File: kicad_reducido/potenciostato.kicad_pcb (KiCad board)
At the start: 2 copper layers, 150 x 100 mm, 35 parts, among them J1 Conn_01x03_Female, J2 USB_B_Micro, J3 Conn_01x03_Male, U1 OP77, U2 TL082, U3 OP77, U4 OP77, U7 TL064

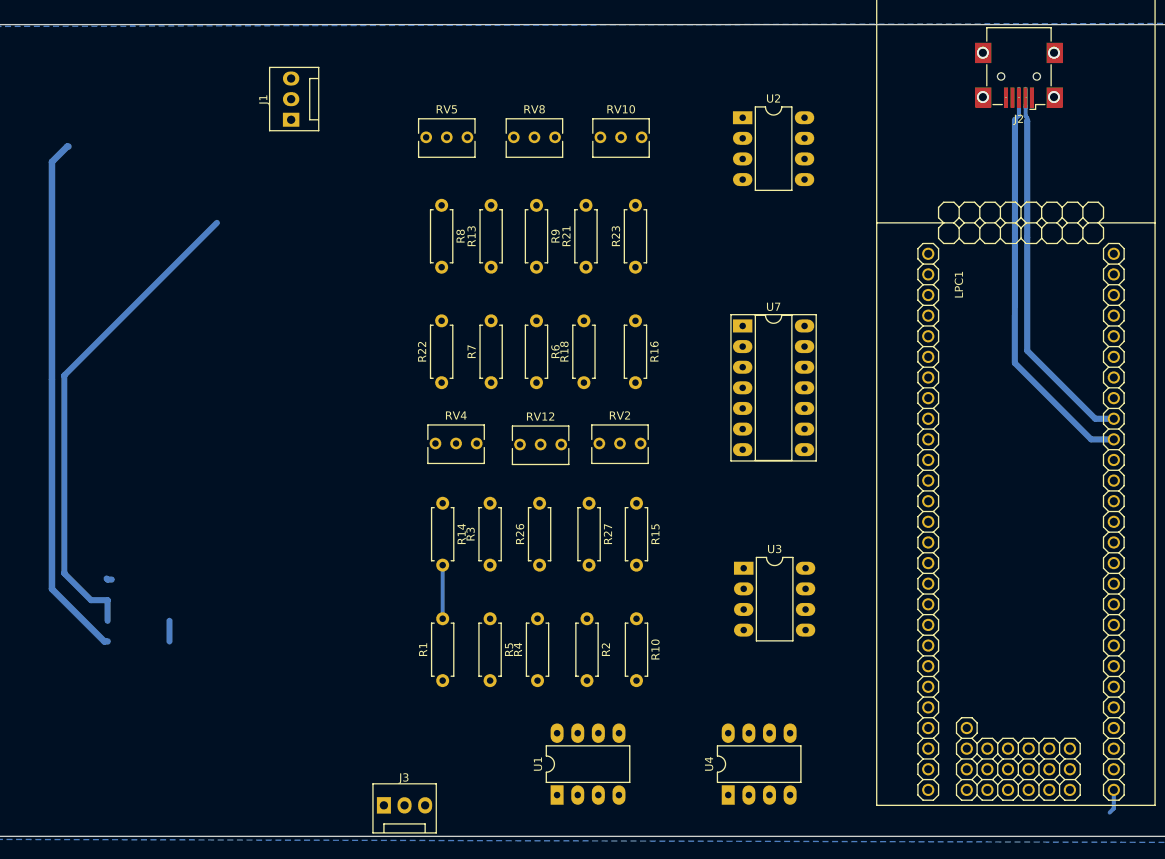
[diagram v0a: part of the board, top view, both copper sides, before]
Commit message: ruteado kicad reducido parcialmente completo
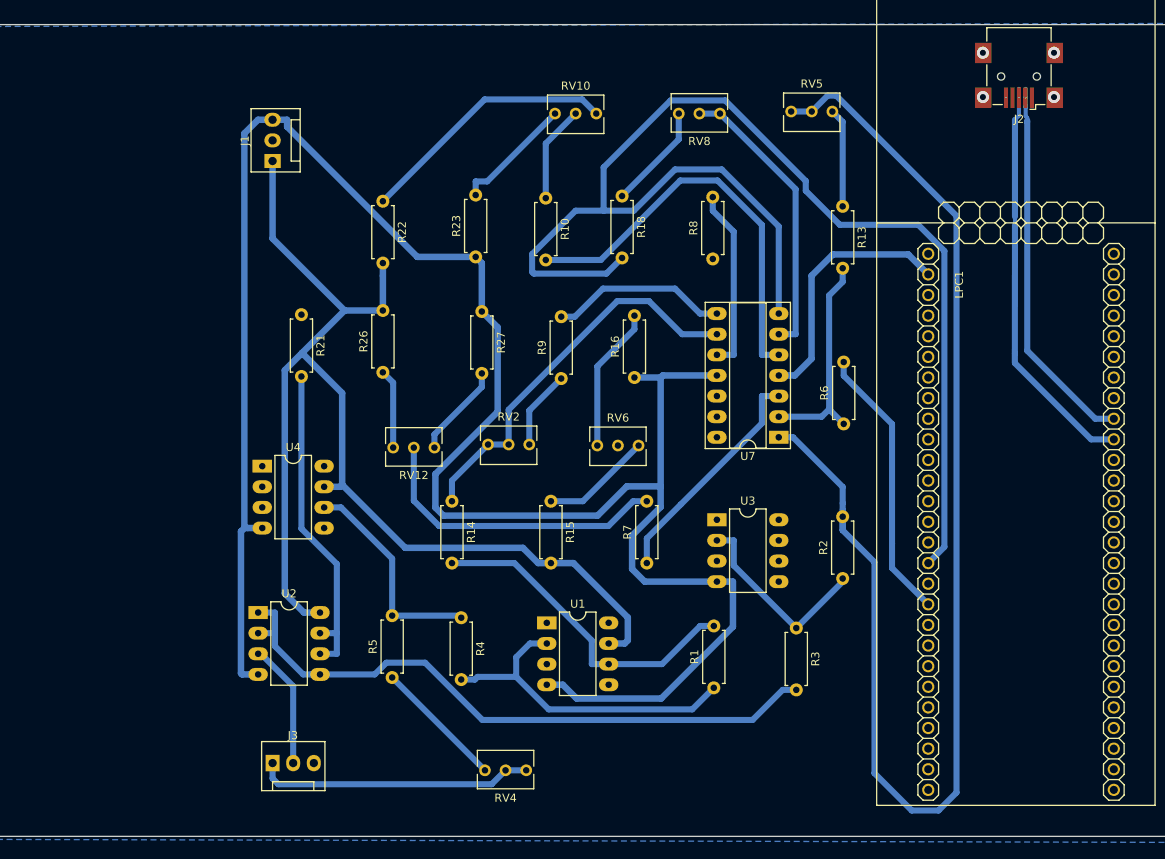
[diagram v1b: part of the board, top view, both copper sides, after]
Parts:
- added RV6: 1K, Potentiometer_THT:Potentiometer_Bourns_3266Y_Vertical, F.Cu at (730.9, 54.4)
- moved U2 85.3 mm to (684.0, 74.9)
- moved U4 70.3 mm to (684.5, 56.9), turned to 0 degrees
- moved R10 53.0 mm to (719.5, 23.9)
- moved RV5 45.1 mm to (754.8, 13.2)
- moved R13 44.0 mm to (756.0, 24.9), turned to 270 degrees
- moved RV4 40.3 mm to (712.0, 94.4), turned to 180 degrees
- moved R6 39.9 mm to (756.2, 51.7), turned to 90 degrees
- moved R3 38.5 mm to (750.3, 76.8), turned to 270 degrees
- moved R21 35.5 mm to (689.4, 38.2), turned to 270 degrees
- moved R8 34.0 mm to (740.0, 31.4), turned to 90 degrees
- moved R1 33.4 mm to (740.2, 84.2)
- moved R2 31.9 mm to (756.0, 70.7), turned to 90 degrees
- moved R26 30.6 mm to (699.4, 45.3)
- moved R7 29.4 mm to (731.9, 68.8)
- moved R27 27.1 mm to (711.6, 37.8)
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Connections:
- LPC1 pad 1: GND -> (no net)
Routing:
- net -5V: track 0.00 -> 253.8 mm
- net /LPC/ADC1: track 0.00 -> 160.9 mm
- net /salida_dac/VIN: track 0.00 -> 160.3 mm
- net +5V: track 65.0 -> 175.4 mm
- net Net-(R3-Pad2): track 3.23 -> 79.0 mm
- net Net-(R10-Pad2): track 0.00 -> 51.0 mm
- net Net-(R14-Pad1): track 0.00 -> 48.5 mm
- net Net-(R10-Pad1): track 60.2 -> 11.9 mm
- net Net-(R1-Pad1): track 0.00 -> 40.9 mm
- net /salida_dac/V_IN: track 0.00 -> 40.1 mm
- net Net-(R7-Pad2): track 0.00 -> 37.8 mm
- net Net-(R21-Pad1): track 0.00 -> 35.7 mm
- net /salida_dac/I_IN: track 6.60 -> 41.1 mm
- net /LPC/DAC: track 0.00 -> 34.2 mm
- net Net-(J3-Pad1): track 0.00 -> 34.1 mm
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
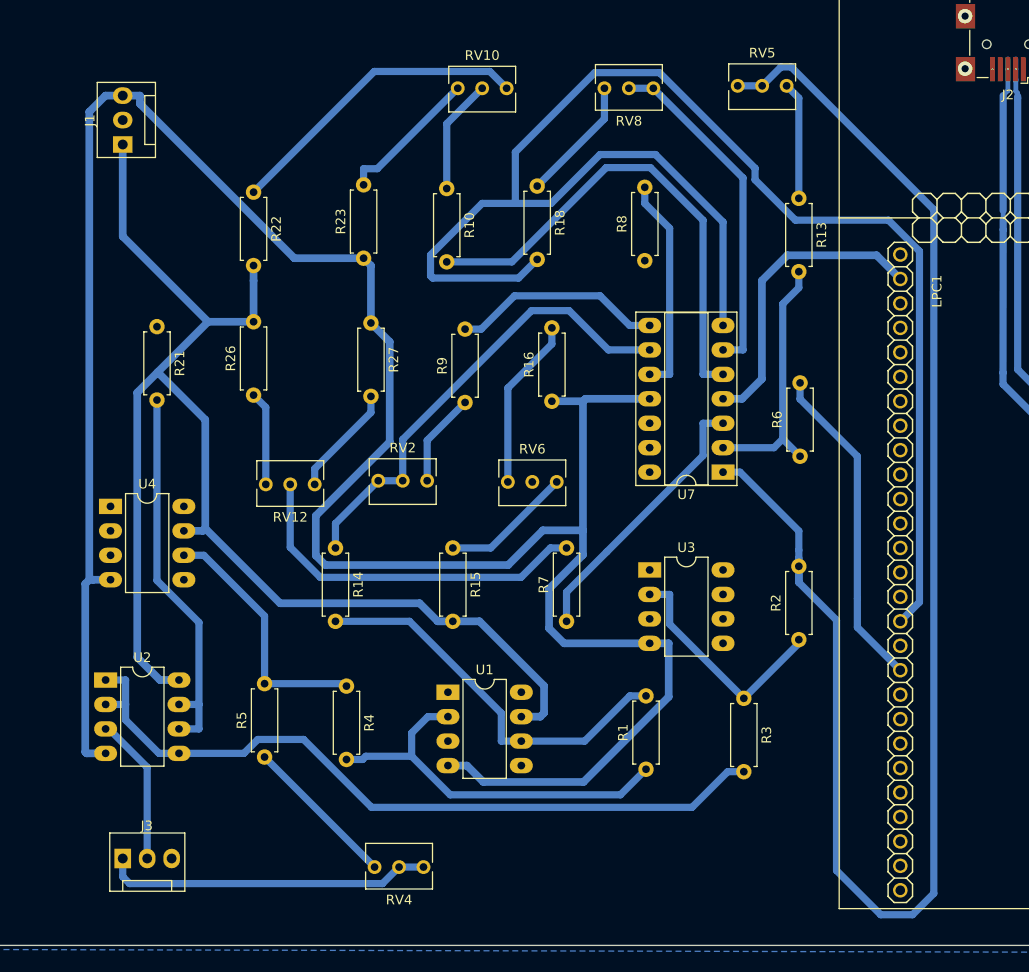
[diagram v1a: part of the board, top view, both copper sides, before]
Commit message: ruteando kicad reducido parte 2
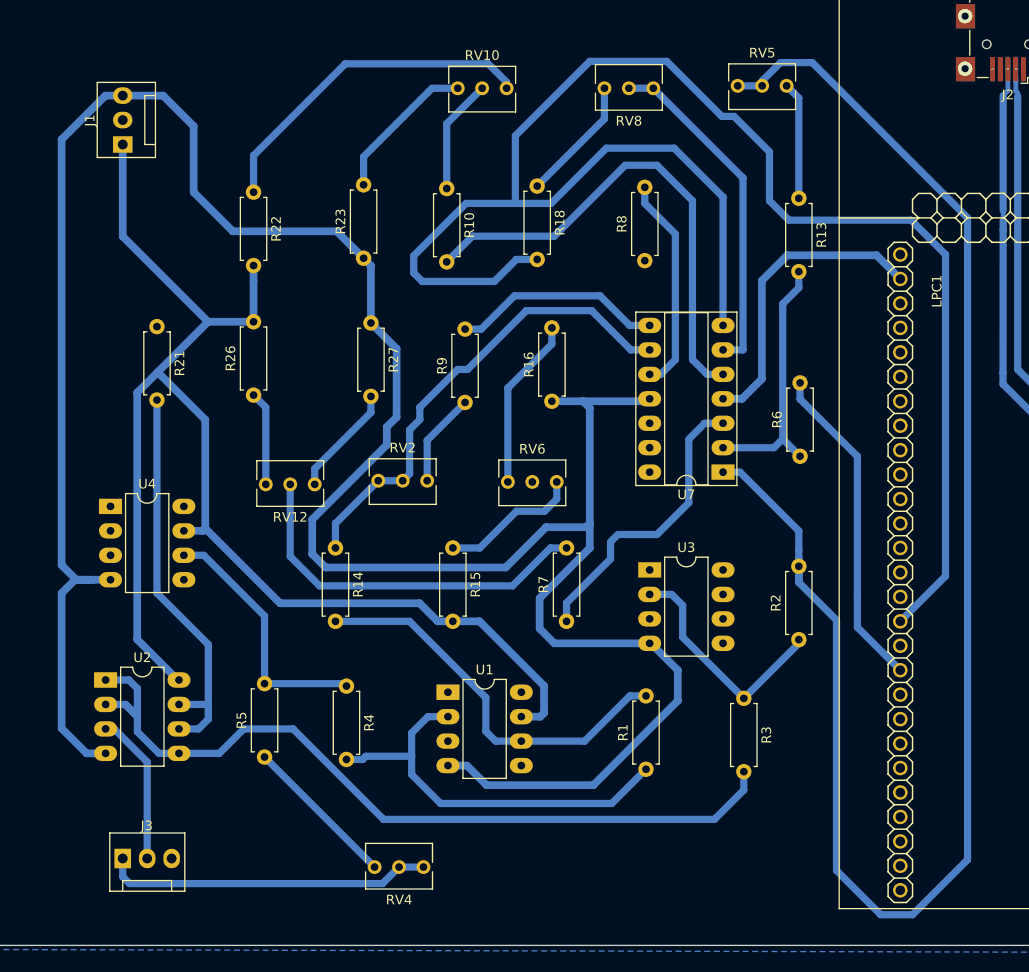
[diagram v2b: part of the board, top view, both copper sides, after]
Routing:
- net -5V: track 253.8 -> 268.3 mm
- net /LPC/ADC1: track 160.9 -> 174.4 mm
- net Net-(R3-Pad2): track 79.0 -> 85.8 mm
- net /salida_dac/VIN: track 160.3 -> 165.4 mm
- net Net-(R22-Pad1): track 32.2 -> 35.5 mm
- net Net-(R7-Pad1): track 28.5 -> 30.6 mm
- net Net-(R1-Pad1): track 40.9 -> 42.8 mm
- net /salida_dac/V_IN: track 40.1 -> 41.8 mm
- net Net-(R7-Pad2): track 37.8 -> 39.1 mm
- net +5V: track 175.4 -> 174.3 mm
- net Net-(R15-Pad1): track 13.6 -> 14.7 mm
- net Net-(R14-Pad1): track 48.5 -> 49.5 mm
- net Net-(R23-Pad2): track 14.9 -> 15.6 mm

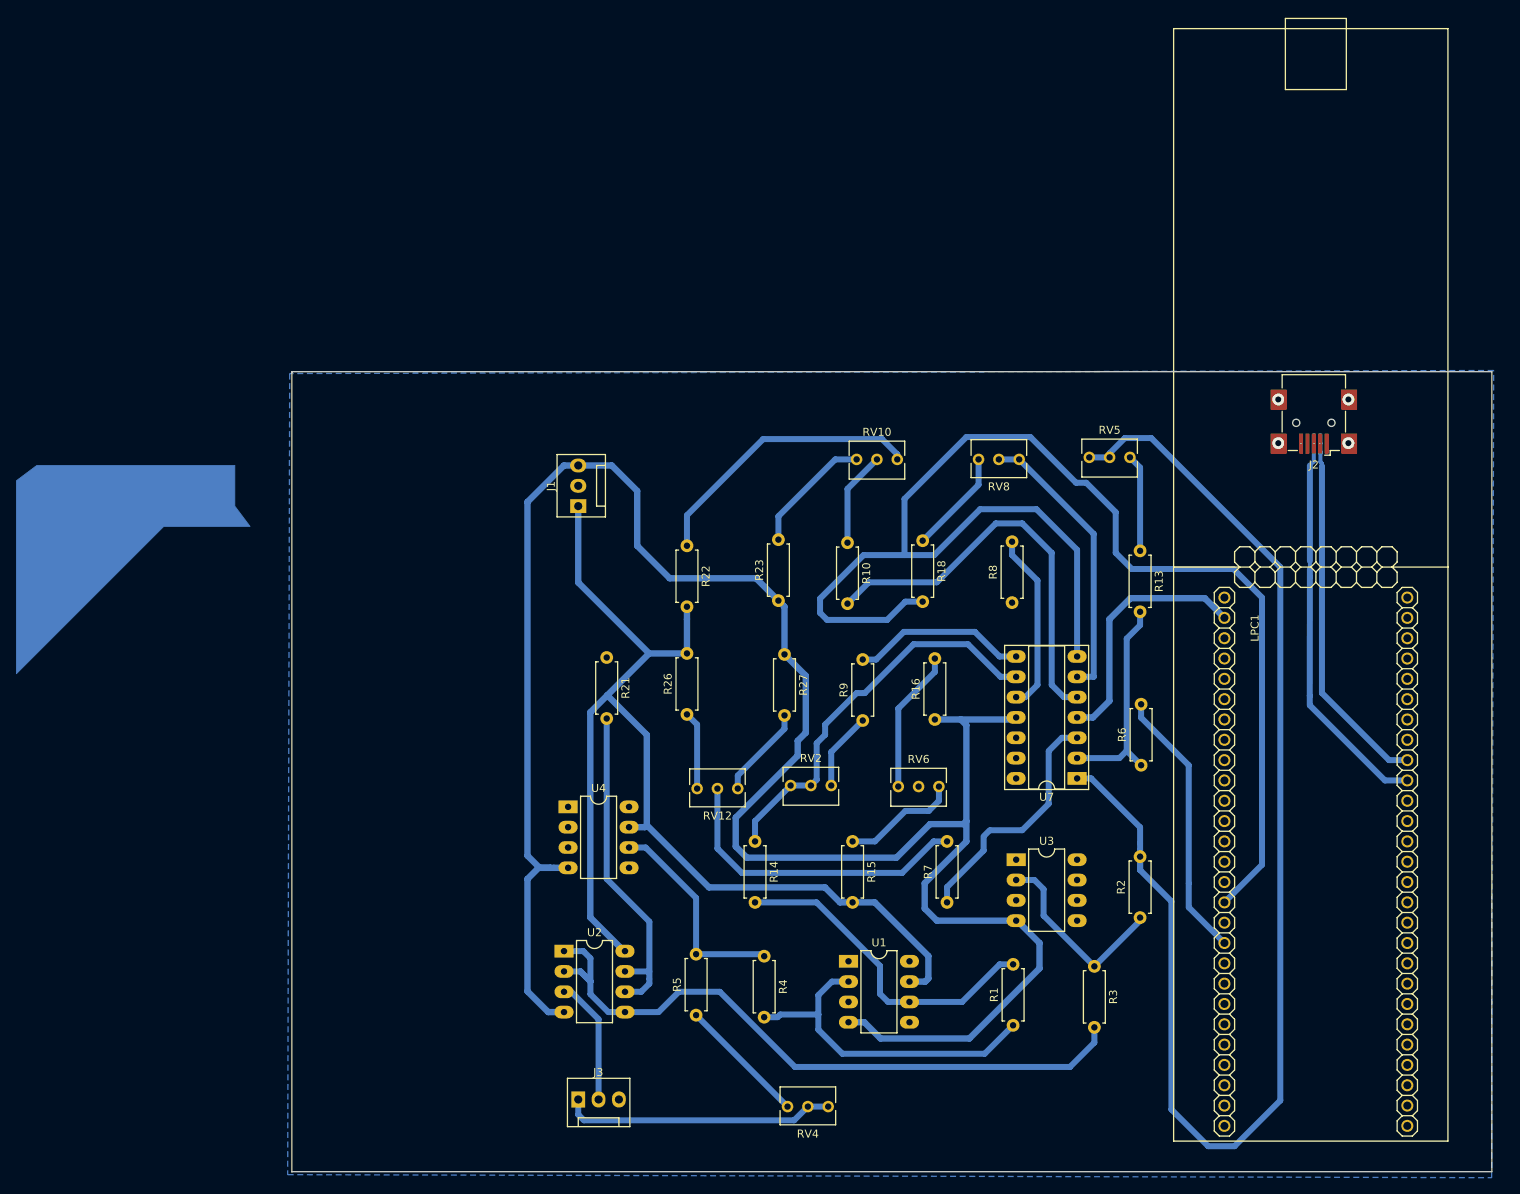
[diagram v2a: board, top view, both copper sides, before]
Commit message: pcb reducido en 10x10
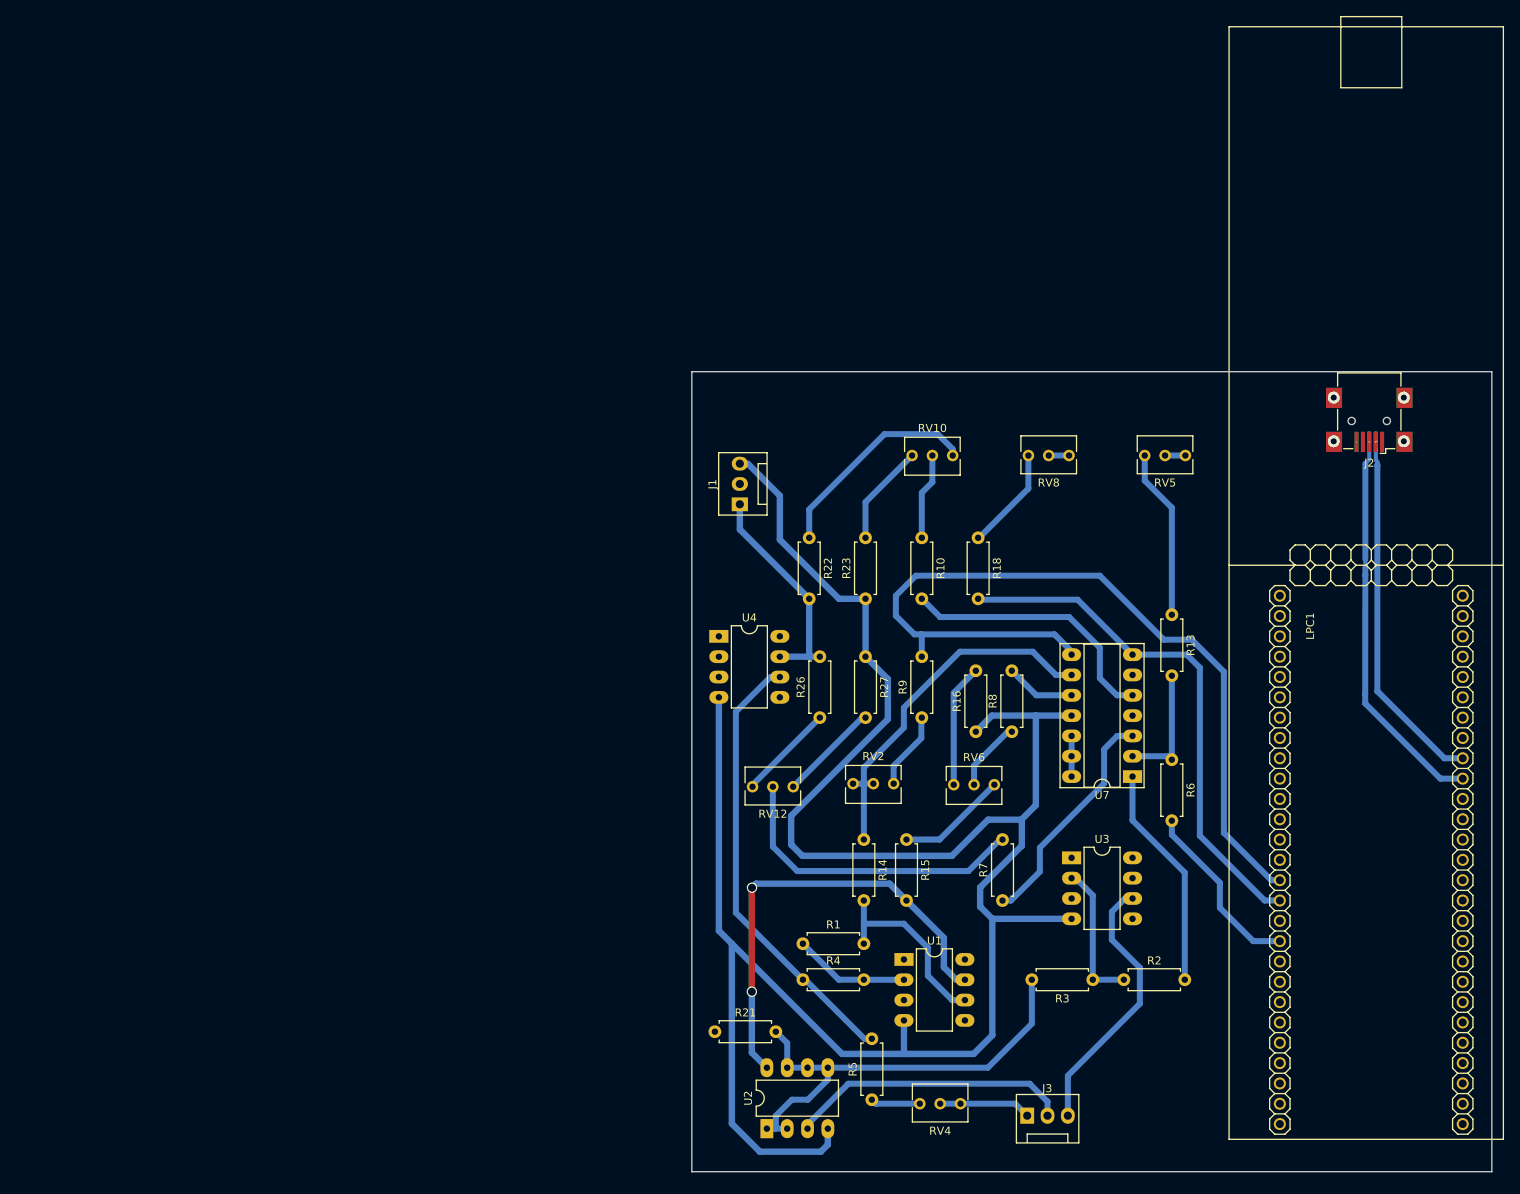
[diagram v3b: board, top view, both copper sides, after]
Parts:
- moved J3 56.2 mm to (741.9, 95.5)
- moved R21 48.7 mm to (702.9, 85.0), turned to 0 degrees
- moved U2 33.7 mm to (709.4, 97.1), turned to 90 degrees
- moved U4 28.5 mm to (703.4, 35.6)
- moved R1 28.2 mm to (713.9, 74.0), turned to 0 degrees
- moved R5 24.4 mm to (722.5, 93.5)
- moved J1 20.2 mm to (706.0, 19.1)
- moved R26 16.6 mm to (716.0, 45.7)
- moved RV4 16.5 mm to (728.5, 94.0)
- moved R8 16.1 mm to (740.0, 47.5)
- moved R22 15.3 mm to (714.7, 23.3)
- moved R14 13.6 mm to (721.5, 61.0)
- moved R23 10.9 mm to (721.7, 30.9)
- moved R27 10.1 mm to (721.7, 38.1)
- moved R10 9.31 mm to (728.7, 23.3)
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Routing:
- net /salida_dac/VIN: track 165.4 -> 30.6 mm
- net /LPC/ADC1: track 174.4 -> 65.6 mm
- net +5V: track 174.3 -> 84.9 mm, vias 0 -> 2
- net /LPC/ADC0: track 21.9 -> 106.1 mm
- net Net-(R3-Pad2): track 85.8 -> 49.8 mm
- net Net-(J3-Pad3): track 0.00 -> 33.9 mm
- net /salida_dac/V_IN: track 41.8 -> 8.39 mm
- net Net-(R21-Pad1): track 35.7 -> 2.54 mm
- net Net-(R4-Pad1): track 26.6 -> 56.5 mm
- net Net-(R1-Pad1): track 42.8 -> 14.5 mm
- net Net-(J3-Pad1): track 34.1 -> 11.5 mm
- net Net-(J3-Pad2): track 15.8 -> 35.3 mm
- net Net-(R10-Pad2): track 51.5 -> 33.6 mm
- net /salida_dac/I_IN: track 41.4 -> 24.2 mm
- net Net-(R8-Pad2): track 22.5 -> 8.74 mm
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- removed copper zone on B.Cu, net GND
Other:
- board size 150 x 100 mm -> 100 x 100 mm
- net class Alimentación: clearance 0.2 -> 0.7; via_dia 0.8 -> 1.3; via_drill 0.4 -> 1
- net class Default: clearance 0.5 -> 0.7
- net class USB: trace_width 0.5 -> 0.75
- rule trace_clearance: 0.5 -> 0.7
